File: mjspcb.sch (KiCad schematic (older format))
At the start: 45 parts, among them P1 Batteries, P10 Lipo, P2 serial breakout, P3 I2C breakout, P4 GPS, P5 piezo, P6 BPW34, P7 electrodes, P8 perfboard breakout, P9 reset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

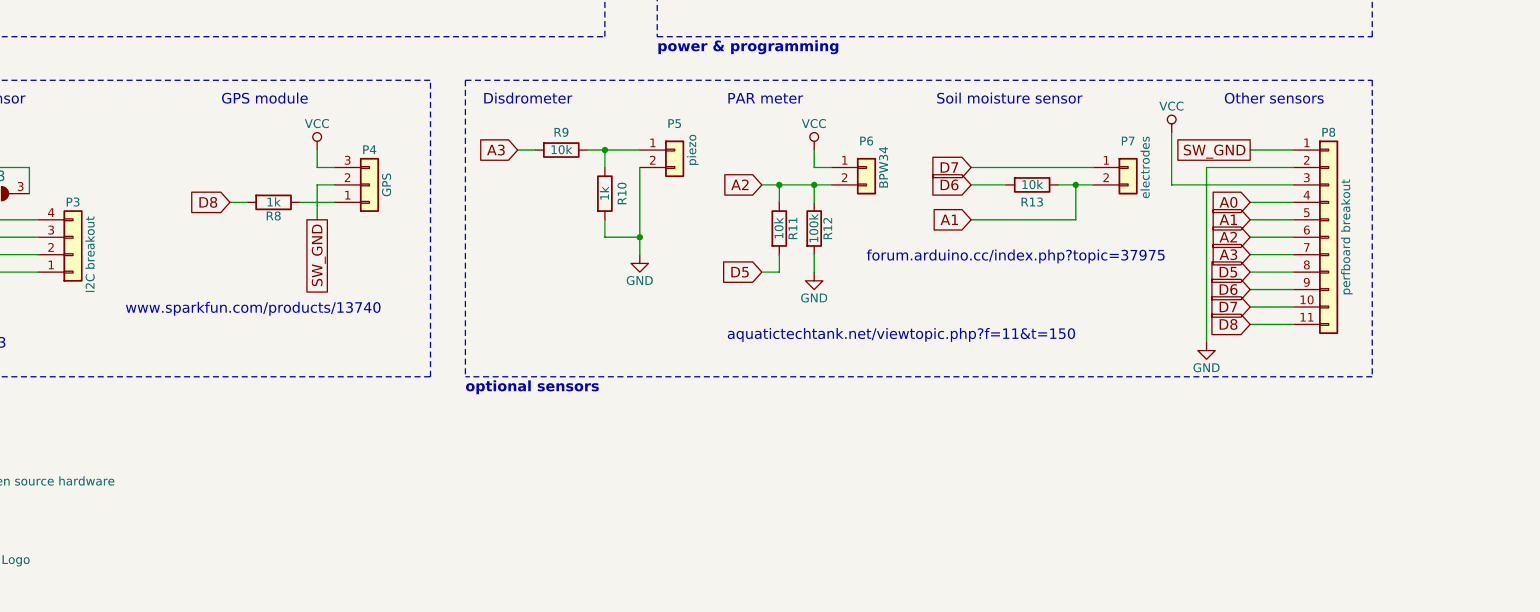
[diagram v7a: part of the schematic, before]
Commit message: Add extra connectors to the board
This adds two connectors for dust sensors (SDS011 and HPMA115S0-XXX) and
two more generic grove connectors (digital and I²C). It also adds a long
pin header with assorted connections (I²C, SPI, various power) for use
with a piggy-back additional PCB which is expected to handle more
complex power needs.

For the grove connectors, some custom experimental footprints are added
that allow using the same footprint for both a 2.0mm grove connector and
a 2.54mm regular pin header.
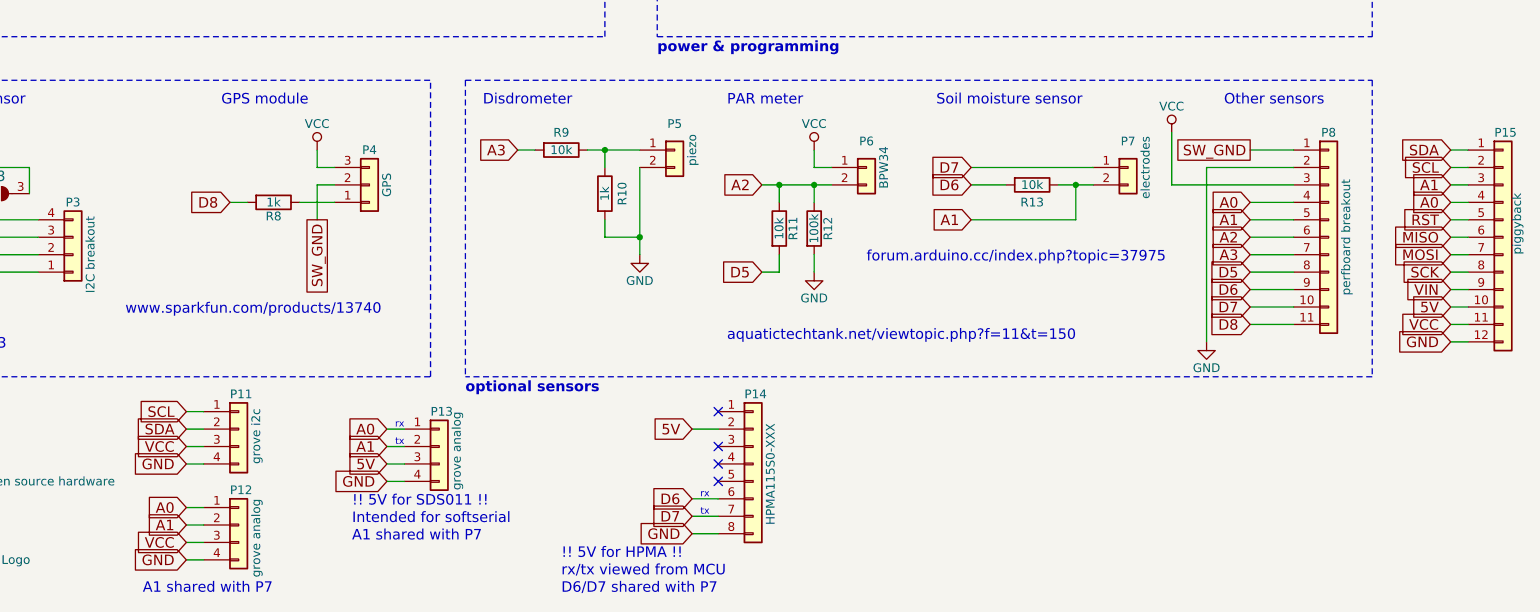
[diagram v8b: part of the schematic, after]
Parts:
- added P11: grove i2c, Connector:NS-Tech_Grove_1x04_P2mm_Vertical, symbol Connector_Generic:Conn_01x04
- added P12: grove analog, meetjestad:NS-Tech_Grove_1x04_P2mm_P2.54mm_Vertical, symbol Connector_Generic:Conn_01x04
- added P13: grove analog, meetjestad:NS-Tech_Grove_1x04_P2mm_P2.54mm_Vertical_Alternative, symbol Connector_Generic:Conn_01x04
- added P14: HPMA115S0-XXX, Connector_Molex:Molex_PicoBlade_53047-0810_1x08_P1.25mm_Vertical, symbol Connector_Generic:Conn_01x08
- added P15: piggyback, Connector_PinHeader_2.54mm:PinHeader_1x12_P2.54mm_Vertical, symbol Connector_Generic:Conn_01x12
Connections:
- net A0: now also P12.1 (Pin_1), P13.1 (Pin_1), P15.4 (Pin_4)
- net A1: now also P12.2 (Pin_2), P13.2 (Pin_2), P15.3 (Pin_3)
- net D6: now also P14.6 (Pin_6)
- net D7: now also P14.7 (Pin_7)
- net GND: now also P11.4 (Pin_4), P12.4 (Pin_4), P13.4 (Pin_4), P14.8 (Pin_8), P15.12 (Pin_12)
- net MISO: now also P15.6 (Pin_6)
- net MOSI: now also P15.7 (Pin_7)
- net RST: now also P15.5 (Pin_5)
- net SCK: now also P15.8 (Pin_8)
- net SCL: now also P11.1 (Pin_1), P15.2 (Pin_2)
- net SDA: now also P11.2 (Pin_2), P15.1 (Pin_1)
- net VCC: now also P11.3 (Pin_3), P12.3 (Pin_3), P15.11 (Pin_11)
- net VIN: now also P15.9 (Pin_9)
- new net 5V: P13.3 (Pin_3), P14.2 (Pin_2), P15.10 (Pin_10)
- no-connect marks 4 -> 8
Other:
- note added: "!! 5V for HPMA !!"
- note added: "!! 5V for SDS011 !!"
- note added: "A1 shared with P7"
- note added: "D6/D7 shared with P7"
- note added: "Intended for softserial"
- note added: "rx"
- note added: "rx/tx viewed from MCU"
- note added: "tx"
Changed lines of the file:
@@
 Wire Wire Line
 	8350 1600 8350 1700
+$Comp
+L Connector_Generic:Conn_01x08 P14
+U 1 1 5C1DCA2A
+P 6650 6900
+F 0 "P14" H 6600 7300 50  0000 L CNN
+F 1 "HPMA115S0-XXX" V 6750 6550 50  0000 L CNN
+F 2 "Connector_Molex:Molex_PicoBlade_53047-0810_1x08_P1.25mm_Vertical" H 6650 6900 50  0001 C CNN
+F 3 "~" H 6650 6900 50  0001 C CNN
+	1    6650 6900
+	1    0    0    -1
+$EndComp
+$Comp
+L Connector_Generic:Conn_01x04 P13
+U 1 1 5C32E565
+P 4850 6800
+F 0 "P13" H 4800 7000 50  0000 L CNN
+F 1 "grove analog" V 4950 6550 50  0000 L CNN
+F 2 "meetjestad:NS-Tech_Grove_1x04_P2mm_P2.54mm_Vertical_Alternative" H 4850 6800 50  0001 C CNN
+F 3 "~" H 4850 6800 50  0001 C CNN
+	1    4850 6800
+	1    0    0    -1
+$EndComp
+Text GLabel 4550 6800 0    60   Input ~ 0
+A1
+Text GLabel 4550 6700 0    60   Input ~ 0
+A0
+Wire Wire Line
+	4550 6700 4650 6700
+Wire Wire Line
+	4650 6800 4550 6800
+Text GLabel 4550 6900 0    60   Input ~ 0
+5V
+Text GLabel 4550 7000 0    60   Input ~ 0
+GND
+Wire Wire Line
+	4550 7000 4650 7000
+Wire Wire Line
+	4550 6900 4650 6900
+$Comp
+L Connector_Generic:Conn_01x04 P11
+U 1 1 5C39D375
+P 3700 6700
+F 0 "P11" H 3650 6900 50  0000 L CNN
+F 1 "grove i2c" V 3800 6500 50  0000 L CNN
+F 2 "Connector:NS-Tech_Grove_1x04_P2mm_Vertical" H 3700 6700 50  0001 C CNN
+F 3 "~" H 3700 6700 50  0001 C CNN
+	1    3700 6700
+	1    0    0    -1
+$EndComp
+Text GLabel 3400 6700 0    60   Input ~ 0
+SDA
+Text GLabel 3400 6600 0    60   Input ~ 0
+SCL
+Wire Wire Line
+	3400 6600 3500 6600
+Wire Wire Line
+	3500 6700 3400 6700
+Text GLabel 3400 6800 0    60   Input ~ 0
+VCC
+Text GLabel 3400 6900 0    60   Input ~ 0
+GND
+Wire Wire Line
+	3400 6900 3500 6900
+Wire Wire Line
+	3400 6800 3500 6800
+$Comp
+L Connector_Generic:Conn_01x04 P12
+U 1 1 5C3A86AF
+P 3700 7250
+F 0 "P12" H 3650 7450 50  0000 L CNN
+F 1 "grove analog" V 3800 6950 50  0000 L CNN
+F 2 "meetjestad:NS-Tech_Grove_1x04_P2mm_P2.54mm_Vertical" H 3700 7250 50  0001 C CNN
+F 3 "~" H 3700 7250 50  0001 C CNN
+	1    3700 7250
+	1    0    0    -1
+$EndComp
+Text GLabel 3400 7250 0    60   Input ~ 0
+A1
+Text GLabel 3400 7150 0    60   Input ~ 0
+A0
+Wire Wire Line
+	3400 7150 3500 7150
+Wire Wire Line
+	3500 7250 3400 7250
+Text GLabel 3400 7350 0    60   Input ~ 0
+VCC
+Text GLabel 3400 7450 0    60   Input ~ 0
+GND
+Wire Wire Line
+	3400 7450 3500 7450
+Wire Wire Line
+	3400 7350 3500 7350
+Text Notes 4350 7150 0    60   ~ 0
+!! 5V for SDS011 !!
+Text Notes 6400 7100 2    39   ~ 0
+rx
+Text Notes 6400 7200 2    39   ~ 0
+tx
+Text GLabel 6300 7300 0    60   Input ~ 0
+GND
+Text GLabel 6300 7200 0    60   Input ~ 0
+D7
+Text GLabel 6300 7100 0    60   Input ~ 0
+D6
+Text GLabel 6300 6700 0    60   Input ~ 0
+5V
+NoConn ~ 6450 6600
+NoConn ~ 6450 6800
+NoConn ~ 6450 6900
+NoConn ~ 6450 7000
+Wire Wire Line
+	6300 6700 6450 6700
+Wire Wire Line
+	6450 7100 6300 7100
+Wire Wire Line
+	6300 7200 6450 7200
+Wire Wire Line
+	6450 7300 6300 7300
+Text Notes 5550 7450 0    60   ~ 0
+!! 5V for HPMA !!
+Text Notes 3150 7650 0    60   ~ 0
+A1 shared with P7
+Text Notes 5550 7550 0    60   ~ 0
+rx/tx viewed from MCU
+Text Notes 4350 7250 0    60   ~ 0
+Intended for softserial
+Text Notes 4650 6700 2    39   ~ 0
+rx
+Text Notes 4650 6800 2    39   ~ 0
+tx
+Text Notes 5550 7650 0    60   ~ 0
+D6/D7 shared with P7
+$Comp
+L Connector_Generic:Conn_01x12 P15
+U 1 1 5C49C38F
+P 10950 5600
+F 0 "P15" H 10900 6200 50  0000 L CNN
+F 1 "piggyback" V 11030 5501 50  0000 L CNN
+F 2 "Connector_PinHeader_2.54mm:PinHeader_1x12_P2.54mm_Vertical" H 10950 5600 50  0001 C CNN
+F 3 "~" H 10950 5600 50  0001 C CNN
+	1    10950 5600
+	1    0    0    -1
+$EndComp
+Text GLabel 10650 6200 0    60   Input ~ 0
+GND
+Text GLabel 10650 6100 0    60   Input ~ 0
+VCC
+Text GLabel 10650 6000 0    60   Input ~ 0
+5V
+Text GLabel 10650 5900 0    60   Input ~ 0
+VIN
+Text GLabel 10650 5800 0    60   Input ~ 0
+SCK
+Text GLabel 10650 5700 0    60   Input ~ 0
+MOSI
+Text GLabel 10650 5600 0    60   Input ~ 0
+MISO
+Text GLabel 10650 5500 0    60   Input ~ 0
+RST
+Text GLabel 10650 5400 0    60   Input ~ 0
+A0
+Text GLabel 10650 5300 0    60   Input ~ 0
+A1
+Text GLabel 10650 5200 0    60   Input ~ 0
+SCL
+Text GLabel 10650 5100 0    60   Input ~ 0
+SDA
+Wire Wire Line
+	10650 5100 10750 5100
+Wire Wire Line
+	10750 5200 10650 5200
+Wire Wire Line
+	10650 5300 10750 5300
+Wire Wire Line
+	10650 5400 10750 5400
+Wire Wire Line
+	10650 5500 10750 5500
+Wire Wire Line
+	10650 5600 10750 5600
+Wire Wire Line
+	10650 5700 10750 5700
+Wire Wire Line
+	10750 5800 10650 5800
+Wire Wire Line
+	10650 5900 10750 5900
+Wire Wire Line
+	10650 6000 10750 6000
+Wire Wire Line
+	10650 6100 10750 6100
+Wire Wire Line
+	10650 6200 10750 6200
+Text Notes 4350 7350 0    60   ~ 0
+A1 shared with P7
 $EndSCHEMATC
